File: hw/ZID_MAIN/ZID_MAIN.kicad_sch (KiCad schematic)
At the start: 182 parts, among them J1 Conn 1x04 0.1" Socket, J10 FFC/FPC-40 Socket, J11 JST-PH-K B6B, J12 JST-PH-K B6B, J13 Conn_02x05_PINHDR_2.54mm, J14 USB-C PWR ONLY, J15 Conn 2x03 pin hdr 0.1", J2 JST-PH-K B6B, J3 Conn 1x02 0.1" pin, J4 Conn 1x03 0.1" pin, J5 Conn 1x08 0.1" pin, J6 Conn 1x08 0.1" pin, J7 Conn 2x04 0.1" pin, J8 Conn 2x02 0.1" pin, J9 Conn 2x04 0.1" pin, M1 WS-RP2040-Zero, SW1 SW_Push, SW2 SW_DIP_x02, U1 OSC-20MHz, U10 27WZ06, U11 74LVC125AS, U12 74LVC273, U13 74FCT2245, U14 AS7C1024B, U15 ATF1508AS, U16 74FCT2245, U17 74HCT166, U18 ATF1508AS, U19 74HCT166, U2 74FCT2245, U20 74FCT2244, U22 ATF1504AS-44T, U23 74AHCT00, U24 74FCT2244, U3 24LC32, U4 MIC2775, U5 SST39SF010, U6 74LVC245, U7 74FCT2245, U8 74AHCT14, U9 Z80 C20MHz-PLCC

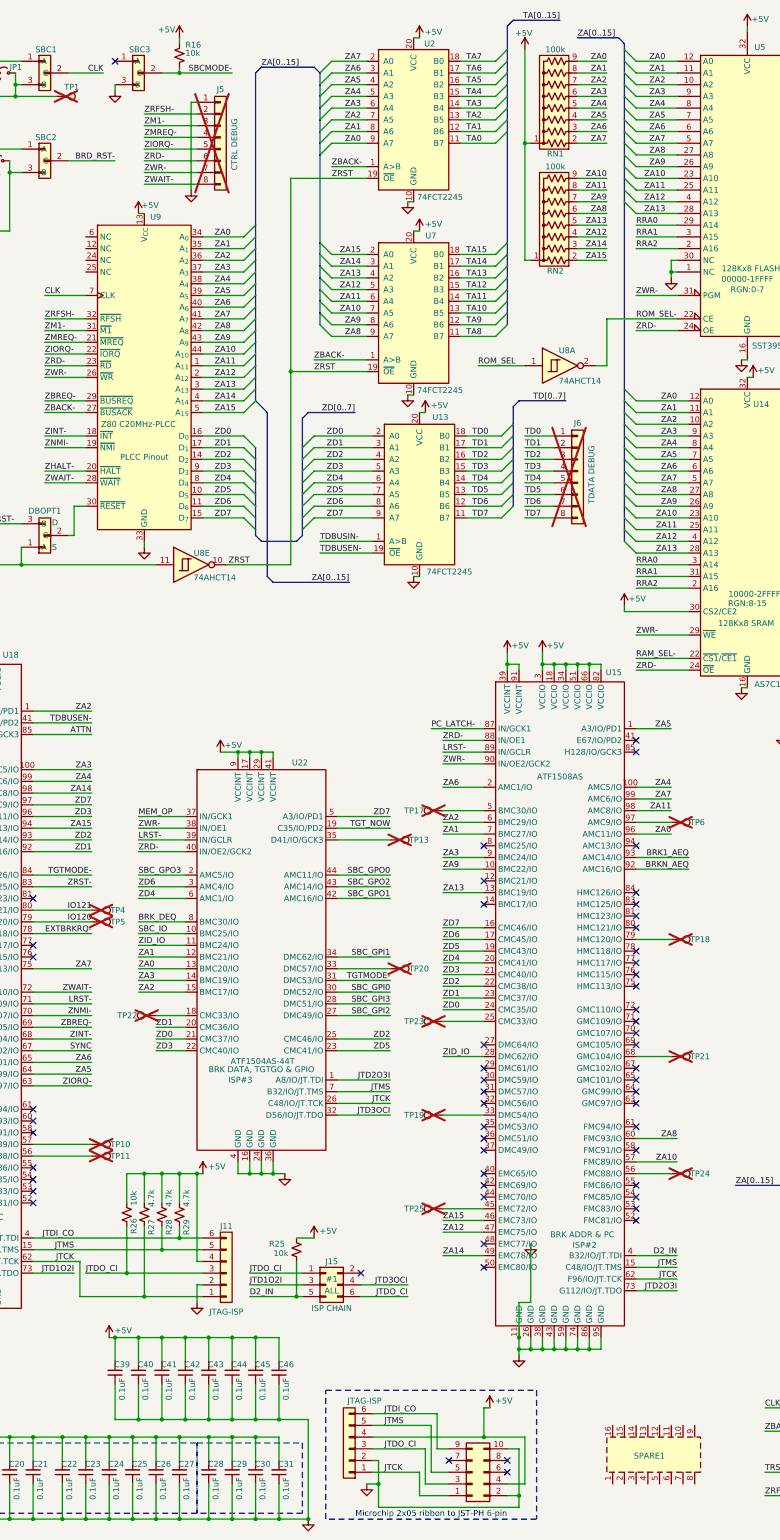
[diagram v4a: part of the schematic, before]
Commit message: PCB: Save before 'rip-out' (3.5x5.0)
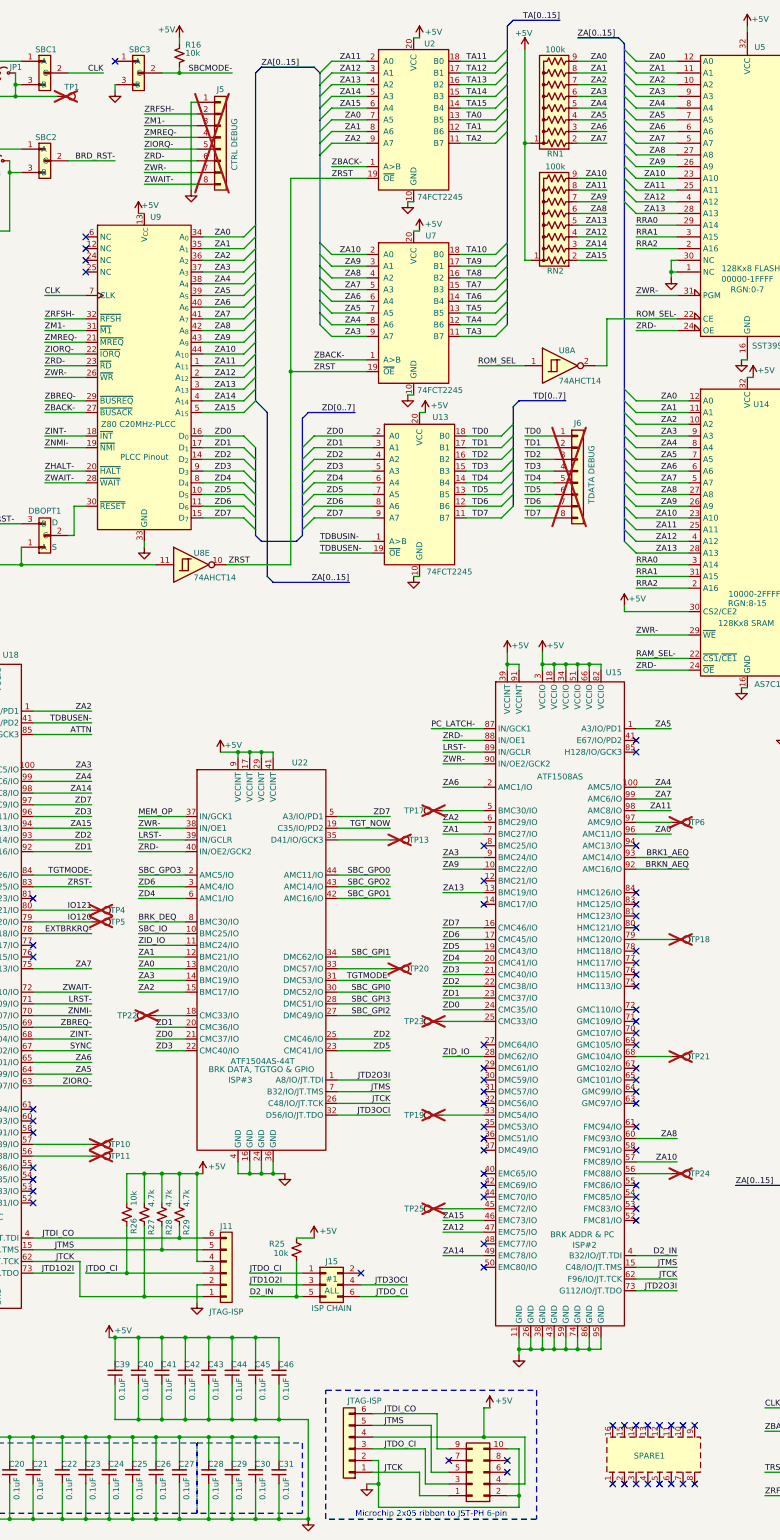
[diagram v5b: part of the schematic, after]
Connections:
- net TA0: now also U2.13 (B5); no longer U2.11 (B7)
- net TA10: now also U7.18 (B0); no longer U7.13 (B5)
- net TA11: now also U2.18 (B0); no longer U7.14 (B4)
- net TA12: now also U2.17 (B1); no longer U7.15 (B3)
- net TA13: now also U2.16 (B2); no longer U7.16 (B2)
- net TA14: now also U2.15 (B3); no longer U7.17 (B1)
- net TA15: now also U2.14 (B4); no longer U7.18 (B0)
- net TA2: now also U2.11 (B7); no longer U2.13 (B5)
- net TA3: now also U7.11 (B7); no longer U2.14 (B4)
- net TA4: now also U7.12 (B6); no longer U2.15 (B3)
- net TA5: now also U7.13 (B5); no longer U2.16 (B2)
- net TA6: now also U7.14 (B4); no longer U2.17 (B1)
- net TA7: now also U7.15 (B3); no longer U2.18 (B0)
- net TA8: now also U7.16 (B2); no longer U7.11 (B7)
- net TA9: now also U7.17 (B1); no longer U7.12 (B6)
- net ZA0: now also U2.7 (A5); no longer U2.9 (A7)
- net ZA10: now also U7.2 (A0); no longer U7.7 (A5)
- net ZA11: now also U2.2 (A0); no longer U7.6 (A4)
- net ZA12: now also U2.3 (A1); no longer U7.5 (A3)
- net ZA13: now also U2.4 (A2); no longer U7.4 (A2)
- net ZA14: now also U2.5 (A3); no longer U7.3 (A1)
- net ZA15: now also U2.6 (A4); no longer U7.2 (A0)
- net ZA2: now also U2.9 (A7); no longer U2.7 (A5)
- net ZA3: now also U7.9 (A7); no longer U2.6 (A4)
- net ZA4: now also U7.8 (A6); no longer U2.5 (A3)
- net ZA5: now also U7.7 (A5); no longer U2.4 (A2)
- net ZA6: now also U7.6 (A4); no longer U2.3 (A1)
- net ZA7: now also U7.5 (A3); no longer U2.2 (A0)
- net ZA8: now also U7.4 (A2); no longer U7.9 (A7)
- net ZA9: now also U7.3 (A1); no longer U7.8 (A6)
- no-connect marks 71 -> 91

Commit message: PCB: Checkpoint... 349 nets left
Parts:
- removed U11: 74LVC125AS, Package_SO:SOIC-14_3.9x8.7mm_P1.27mm, symbol 74xx:74LVC125
- added U11, U21: 74LVC2G34, Package_TO_SOT_SMD:SOT-23-6, symbol AES_Library:74LVC2G34-AES
- R12, R16, R24, R31, R38, R39, R8, R9: value 10k -> 20k
- U10: value 27WZ06 -> 74LVC2G06; Alternate (none) -> 27WZ06
- U3: value 24LC32 -> 24LC32A EEP
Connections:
- net +3.3V: now also U11.5 (VCC), U21.5 (VCC)
- net GND: now also U11.2 (GND), U21.2 (GND)
- net LRST-: now also U21.3
- net MA0: now also U11.4
- net MOD_SEL-: now also U21.1; no longer U6.19 (~{OE})
- net MRD-: now also U6.1 (A>B), U11.6
- net MRST-: now also U21.4
- net MSEL-: now also U6.19 (~{OE}), U21.6
- net TA0: now also U2.16 (B2); no longer U2.13 (B5)
- net TA1: now also U2.17 (B1); no longer U2.12 (B6)
- net TA11: now also U2.11 (B7); no longer U2.18 (B0)
- net TA12: now also U2.12 (B6); no longer U2.17 (B1)
- net TA13: now also U2.13 (B5); no longer U2.16 (B2)
- net TA14: now also U2.14 (B4); no longer U2.15 (B3)
- net TA15: now also U2.15 (B3); no longer U2.14 (B4)
- net TA2: now also U2.18 (B0); no longer U2.11 (B7)
- net ZA0: now also U2.4 (A2), U11.3; no longer U2.7 (A5)
- net ZA1: now also U2.3 (A1); no longer U2.8 (A6)
- net ZA11: now also U2.9 (A7); no longer U2.2 (A0)
- net ZA12: now also U2.8 (A6); no longer U2.3 (A1)
- net ZA13: now also U2.7 (A5); no longer U2.4 (A2)
- net ZA14: now also U2.6 (A4); no longer U2.5 (A3)
- net ZA15: now also U2.5 (A3); no longer U2.6 (A4)
- net ZA2: now also U2.2 (A0); no longer U2.9 (A7)
- net ZRD-: now also U11.1; no longer U6.1 (A>B)
- net at LED4.2 (A): now also U12.12 (Q4); no longer U12.16 (Q6)
- net at LED2.2 (A): now also U12.16 (Q6); no longer U12.12 (Q4)
- net at LED5.1 (K): now also U12.9 (Q3); no longer U12.19 (Q7)
- net at LED1.2 (A): now also U12.19 (Q7); no longer U12.9 (Q3)
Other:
- moved on the sheet: LED1, LED2, LED3, LED4, LED5, R11, R12, R13, R15, R17, R18, U10C

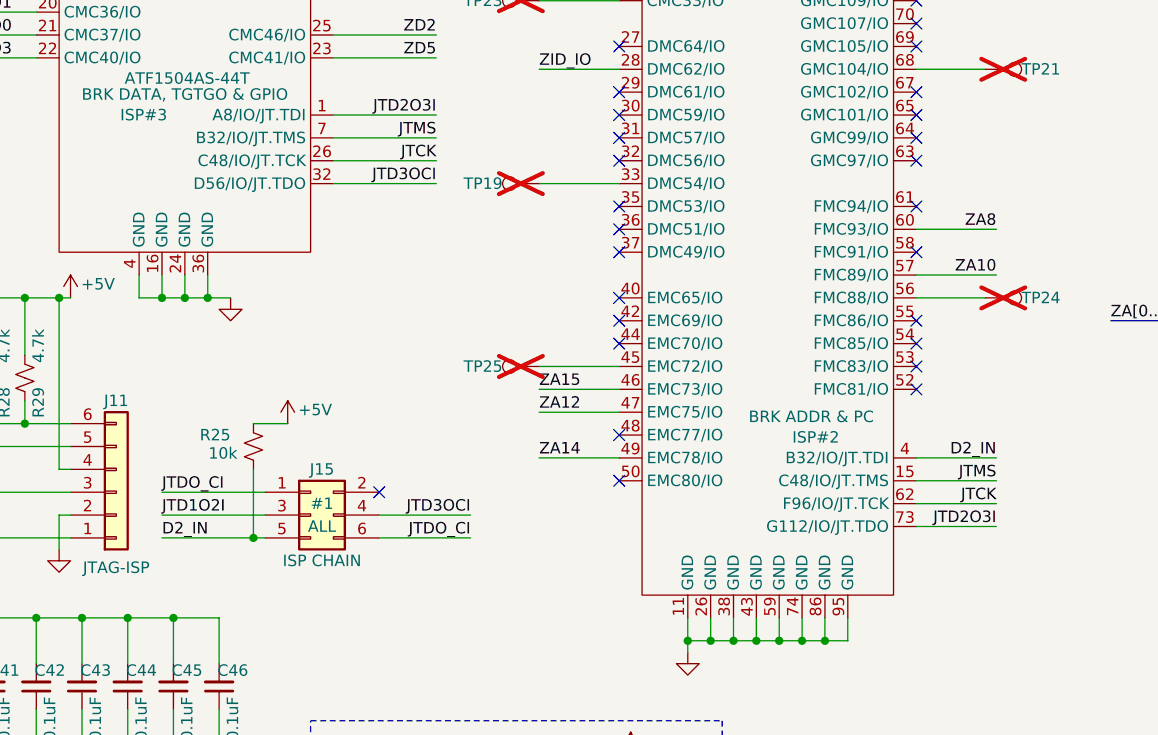
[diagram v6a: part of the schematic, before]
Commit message: Checkpoint after removing JTAG-ISP Chain header (J15)
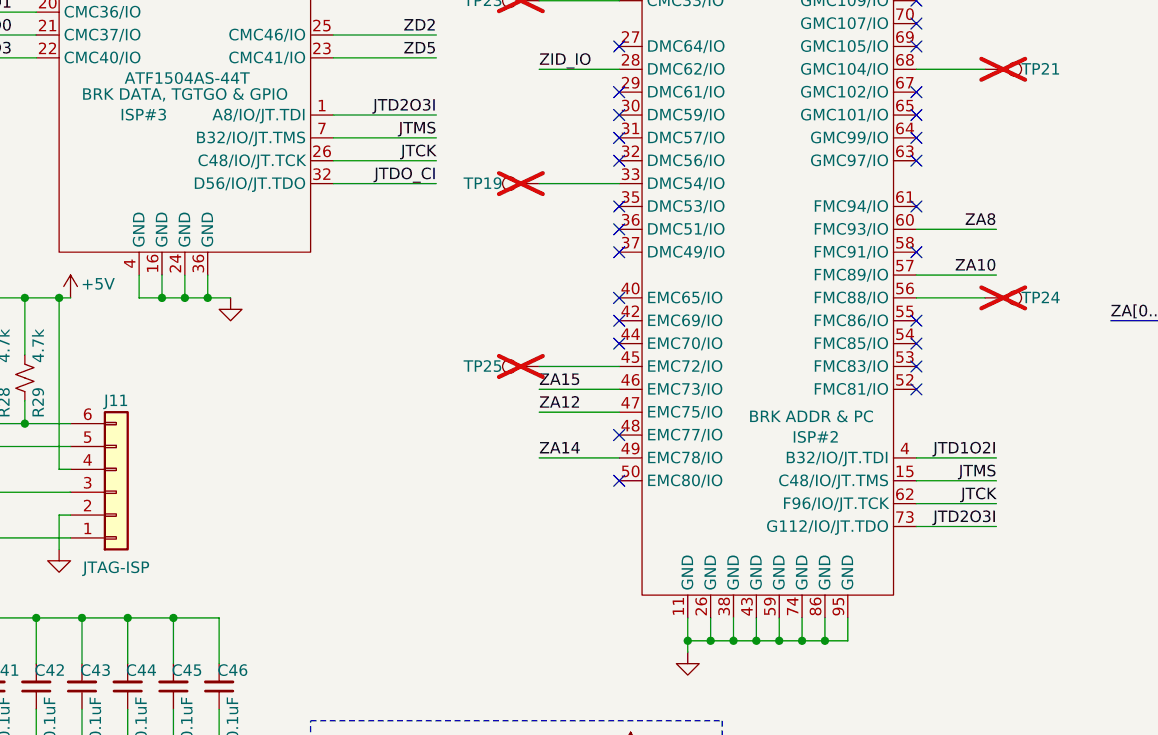
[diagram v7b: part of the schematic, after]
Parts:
- removed J15: Conn 2x03 pin hdr 0.1", Connector_PinHeader_2.00mm:PinHeader_2x03_P2.00mm_Vertical, symbol Connector_Generic:Conn_02x03_Odd_Even
- removed R25: 10k, Resistor_SMD:R_0805_2012Metric, symbol Device:R_Small_US
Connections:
- net D2_IN is gone; now on net JTD1O2I: U15.4 (B32/IO/JT.TDI)
- net JTD3OCI is gone; now on net JTDO_CI: U22.32 (D56/IO/JT.TDO)
- no-connect marks 91 -> 90

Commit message: Checkpoint - Routing PWR/GND
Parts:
- removed TP2: TestPoint, TestPoint:TestPoint_THTPad_D1.0mm_Drill0.5mm, symbol Connector:TestPoint
- DBOPT1: Function DB RST -> RST(ZDB); OP1-2 S -> STD; OP2-3 D -> DZ
- OP2: OP-A P-WAIT -> YES
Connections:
- net IOE1: no longer names the net of U18.88 (IN/OE1)
- no-connect marks 90 -> 91
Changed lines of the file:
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@@
 	)
 	(no_connect
+		(at 27.94 162.56)
+	)
+	(no_connect
 		(at 158.75 262.89)
 	)
@@
 	(wire
 		(pts
-			(xy 13.97 162.56) (xy 27.94 162.56)
-		)
-		(stroke
-			(width 0)
-			(type default)
-		)
-	)
-	(wire
-		(pts
 			(xy 284.48 289.56) (xy 285.75 289.56)
 		)
@@
 		)
 	)
-	(label "IOE1"
-		(at 15.24 162.56 0)
-		(effects
-			(font
-				(size 1.27 1.27)
-			)
-			(justify left bottom)
-		)
-	)
 	(label "ZA3"
 		(at 132.08 78.74 180)
@@
 			)
 		)
-		(property "OP-A" "P-WAIT"
+		(property "OP-A" "YES"
 			(at 347.98 243.84 0)
 			(effects
@@
 			)
 		)
-		(property "Function" "DB RST"
+		(property "Function" "RST(ZDB)"
 			(at 61.722 121.666 0)
 			(effects
@@
 			)
 		)
-		(property "OP1-2" "S"
+		(property "OP1-2" "STD"
 			(at 65.024 124.46 0)
 			(effects
@@
 			)
 		)
-		(property "OP2-3" "D"
+		(property "OP2-3" "DZ"
 			(at 65.024 119.126 0)
 			(effects
@@
 					(unit 1)
 				)
-			)
-		)
-	)
-	(symbol
-		(lib_id "Connector:TestPoint")
-		(at 13.97 162.56 90)
-		(unit 1)
-		(exclude_from_sim no)
-		(in_bom no)
-		(on_board yes)
-		(dnp yes)
-		(property "Reference" "TP2"
-			(at 10.668 160.528 90)
-			(effects
-				(font
-					(size 1.27 1.27)
-				)
-			)
-		)
-		(property "Value" "TestPoint"
-			(at 10.668 160.02 90)
-			(effects
-				(font
-					(size 1.27 1.27)
-				)
-				(hide yes)
-			)
-		)
-		(property "Footprint" "TestPoint:TestPoint_THTPad_D1.0mm_Drill0.5mm"
-			(at 13.97 157.48 0)
-			(effects
-				(font
-					(size 1.27 1.27)
-				)
-				(hide yes)
-			)
-		)
-		(property "Datasheet" "~"
-			(at 13.97 157.48 0)
-			(effects
-				(font
-					(size 1.27 1.27)
-				)
-				(hide yes)
-			)
-		)
-		(property "Description" "test point"
-			(at 13.97 162.56 0)
-			(effects
-				(font
-					(size 1.27 1.27)
-				)
-				(hide yes)
-			)
-		)
-		(property "Function" "IO1"
-			(at 13.97 162.56 90)
-			(effects
-				(font
-					(size 1.27 1.27)
-				)
-				(hide yes)
-			)
-		)
-		(pin "1"
-		)
-		(instances
-			(project "ZID_MAIN"
-				(path "/2be47242-6db6-4d8d-b590-8c682dee013e"
-					(reference "TP2")
-					(unit 1)
-				)
